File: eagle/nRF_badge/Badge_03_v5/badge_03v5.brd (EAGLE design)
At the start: 30 x 70 mm, 45 parts, among them U2 LP2985LV, U3 MCP6231, U4 PCF85263, U5 M95M02, Y1 32768Hz, Y2 32768Hz

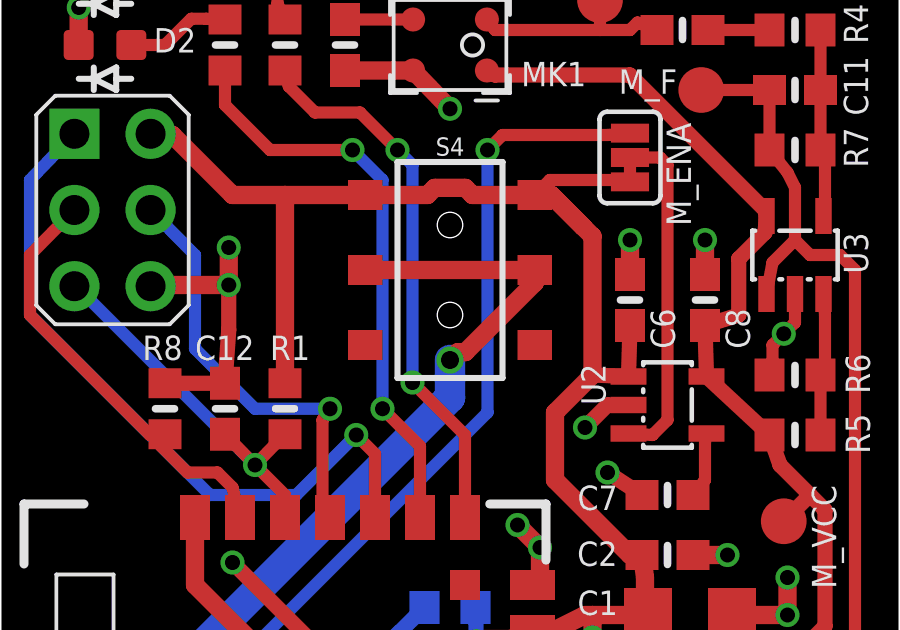
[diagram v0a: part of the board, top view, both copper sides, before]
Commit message: Changed power traces in 3v05
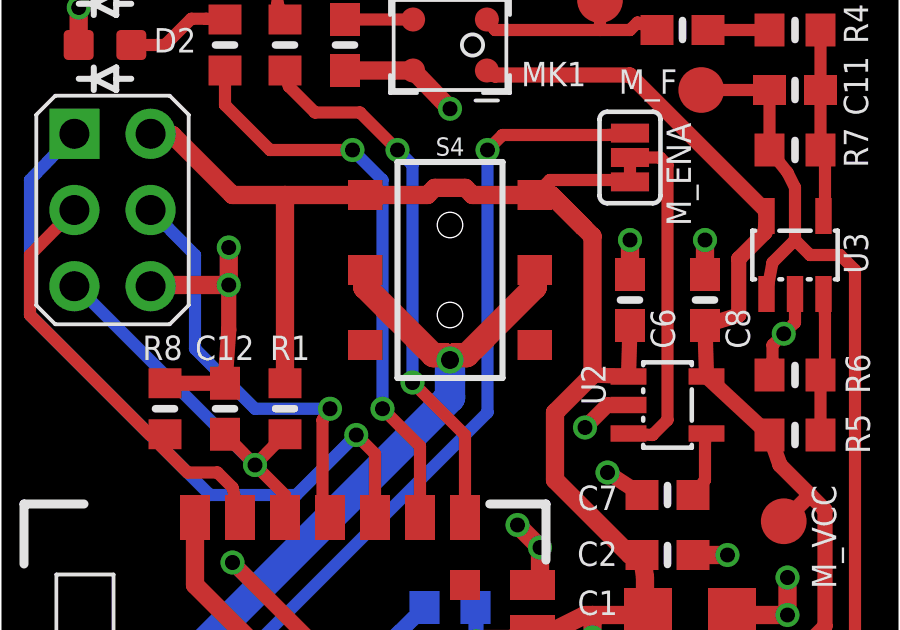
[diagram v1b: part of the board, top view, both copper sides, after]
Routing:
- net VBATT: track 161.1 -> 160.0 mm
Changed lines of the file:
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@@
 <grid distance="0.125" unitdist="mm" unit="mm" style="lines" multiple="4" display="yes" altdistance="0.000000123031" altunitdist="inch" altunit="inch"/>
 <layers>
-<layer number="1" name="Top" color="4" fill="1" visible="no" active="yes"/>
+<layer number="1" name="Top" color="4" fill="1" visible="yes" active="yes"/>
 <layer number="16" name="Bottom" color="1" fill="1" visible="yes" active="yes"/>
 <layer number="17" name="Pads" color="2" fill="1" visible="yes" active="yes"/>
@@
 <layer number="19" name="Unrouted" color="14" fill="1" visible="yes" active="yes"/>
 <layer number="20" name="Dimension" color="15" fill="1" visible="yes" active="yes"/>
-<layer number="21" name="tPlace" color="16" fill="1" visible="no" active="yes"/>
+<layer number="21" name="tPlace" color="16" fill="1" visible="yes" active="yes"/>
 <layer number="22" name="bPlace" color="7" fill="1" visible="yes" active="yes"/>
-<layer number="23" name="tOrigins" color="15" fill="1" visible="no" active="yes"/>
+<layer number="23" name="tOrigins" color="15" fill="1" visible="yes" active="yes"/>
 <layer number="24" name="bOrigins" color="15" fill="1" visible="yes" active="yes"/>
-<layer number="25" name="tNames" color="7" fill="1" visible="no" active="yes"/>
+<layer number="25" name="tNames" color="7" fill="1" visible="yes" active="yes"/>
 <layer number="26" name="bNames" color="7" fill="1" visible="yes" active="yes"/>
-<layer number="27" name="tValues" color="7" fill="1" visible="no" active="yes"/>
-<layer number="28" name="bValues" color="7" fill="1" visible="no" active="yes"/>
+<layer number="27" name="tValues" color="7" fill="1" visible="yes" active="yes"/>
+<layer number="28" name="bValues" color="7" fill="1" visible="yes" active="yes"/>
 <layer number="29" name="tStop" color="7" fill="3" visible="no" active="yes"/>
 <layer number="30" name="bStop" color="7" fill="6" visible="no" active="yes"/>
@@
 <layer number="37" name="tTest" color="7" fill="1" visible="no" active="yes"/>
 <layer number="38" name="bTest" color="7" fill="1" visible="no" active="yes"/>
-<layer number="39" name="tKeepout" color="4" fill="11" visible="no" active="yes"/>
+<layer number="39" name="tKeepout" color="4" fill="11" visible="yes" active="yes"/>
 <layer number="40" name="bKeepout" color="1" fill="11" visible="yes" active="yes"/>
-<layer number="41" name="tRestrict" color="4" fill="10" visible="no" active="yes"/>
+<layer number="41" name="tRestrict" color="4" fill="10" visible="yes" active="yes"/>
 <layer number="42" name="bRestrict" color="1" fill="10" visible="yes" active="yes"/>
 <layer number="43" name="vRestrict" color="2" fill="10" visible="no" active="yes"/>
-<layer number="44" name="Drills" color="7" fill="1" visible="no" active="yes"/>
+<layer number="44" name="Drills" color="7" fill="1" visible="yes" active="yes"/>
 <layer number="45" name="Holes" color="7" fill="1" visible="yes" active="yes"/>
 <layer number="46" name="Milling" color="3" fill="1" visible="no" active="yes"/>
@@
 <layer number="49" name="Reference" color="7" fill="1" visible="no" active="yes"/>
 <layer number="50" name="dxf" color="7" fill="1" visible="no" active="no"/>
-<layer number="51" name="tDocu" color="6" fill="1" visible="no" active="yes"/>
+<layer number="51" name="tDocu" color="6" fill="1" visible="yes" active="yes"/>
 <layer number="52" name="bDocu" color="6" fill="1" visible="yes" active="yes"/>
 <layer number="53" name="tGND_GNDA" color="7" fill="9" visible="no" active="no"/>
@@
 <contactref element="S4" pad="2"/>
 <contactref element="S4" pad="5"/>
-<wire x1="17.825" y1="53" x2="12.175" y2="53" width="0.6096" layer="1"/>
-<wire x1="15" y1="50" x2="15.2622" y2="50.2622" width="0.6096" layer="1"/>
-<wire x1="15.2622" y1="50.2622" x2="15.51271875" y2="50.2622" width="0.6096" layer="1"/>
-<wire x1="15.51271875" y1="50.2622" x2="17.825" y2="52.57448125" width="0.6096" layer="1"/>
-<wire x1="17.825" y1="52.57448125" x2="17.825" y2="53" width="0.6096" layer="1"/>
+<wire x1="15.1606" y1="50.1606" x2="15" y2="50" width="0.8128" layer="1"/>
+<wire x1="15.1606" y1="50.1606" x2="15.5548" y2="50.1606" width="0.8128" layer="1"/>
+<wire x1="15.5548" y1="50.1606" x2="17.825" y2="52.4308" width="0.8128" layer="1"/>
+<wire x1="17.825" y1="52.4308" x2="17.825" y2="53" width="0.8128" layer="1"/>
+<wire x1="15" y1="50" x2="14.8394" y2="50.1606" width="0.8128" layer="1"/>
+<wire x1="14.8394" y1="50.1606" x2="14.4452" y2="50.1606" width="0.8128" layer="1"/>
+<wire x1="14.4452" y1="50.1606" x2="12.175" y2="52.4308" width="0.8128" layer="1"/>
+<wire x1="12.175" y1="52.4308" x2="12.175" y2="53" width="0.8128" layer="1"/>
 </signal>
 <signal name="MOSI">
